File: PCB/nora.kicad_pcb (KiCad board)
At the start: 2 copper layers, 285 x 95.1 mm, 232 parts, among them J1 USB_C_Receptacle_USB2.0, J2 Conn_01x04, J3 Conn_01x02, J5 Conn_02x03_Odd_Even, U1 ATmega32U4-MU, U2 24LC64, U4 Pico, Y1 16MHz

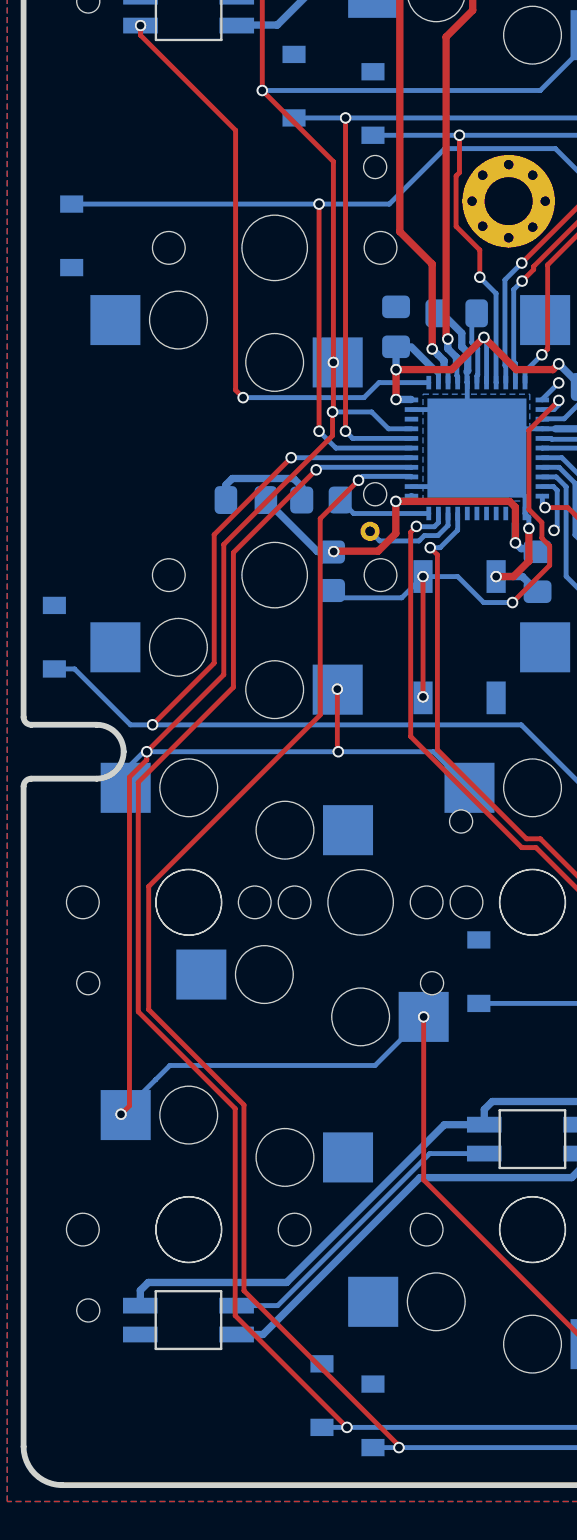
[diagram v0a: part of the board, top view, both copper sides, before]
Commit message: パスコンとRを入れ替えて、パスコンをMCUに近づけた#25
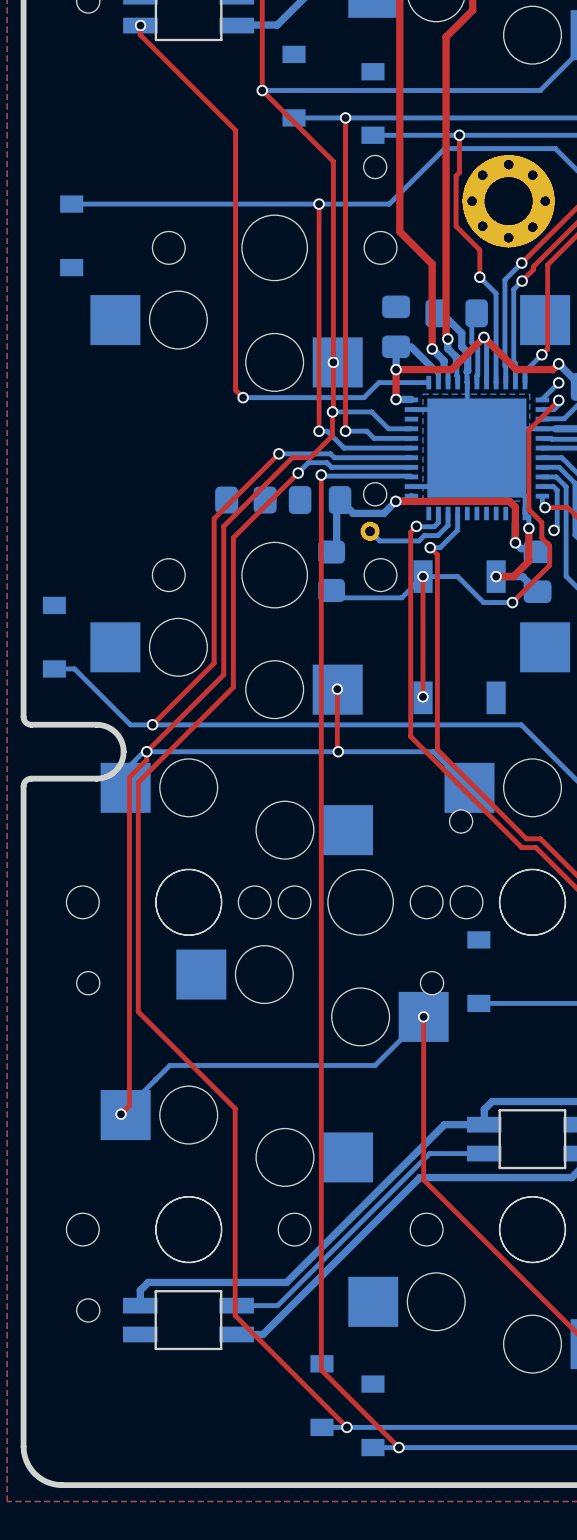
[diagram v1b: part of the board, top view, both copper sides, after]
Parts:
- moved R6 3.90 mm to (34.1, 66.0)
- moved C5 3.85 mm to (38.0, 66.0)
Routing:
- net row9: track 330.3 -> 324.2 mm
- net GND: track 612.4 -> 606.7 mm
- net Net-(R6-Pad2): track 4.89 -> 0.00 mm
- net +5V: track 88.9 -> 85.3 mm, vias 9 -> 8
- net row7: track 310.8 -> 311.4 mm
- net row4: track 338.1 -> 338.7 mm
- net col0: track 166.4 -> 166.9 mm

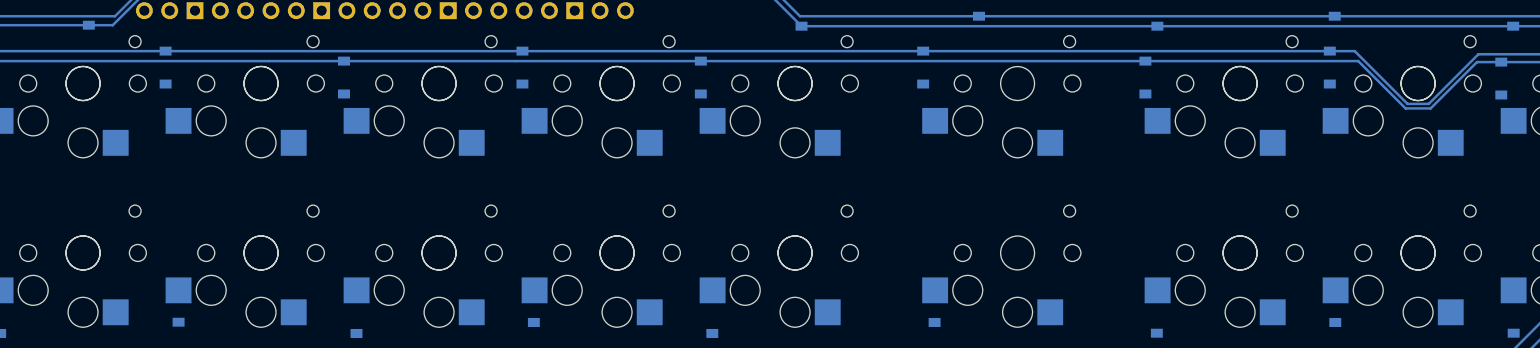
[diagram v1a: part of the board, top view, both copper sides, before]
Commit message: 中央、右上のネジ穴にかぶるスイッチにシルクを追加#14
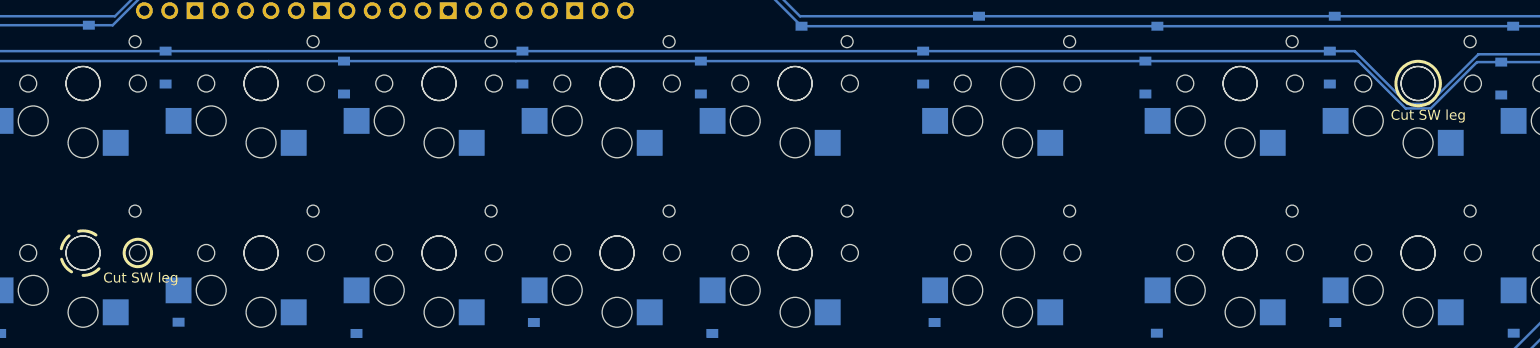
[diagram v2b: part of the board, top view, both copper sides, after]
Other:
- board text added: "Cut SW leg"

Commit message: URL added.#20
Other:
- board text added: "#Nora_kbd v.0.1 by @jpskenn, https://git.io/nora_kbd"
- board text removed: "#Nora_kbd v.0.1, by @jpskenn"

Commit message: Update and Change version information.#18#21
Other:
- board text added: "#Nora_kbd DN0020 by @jpskenn, https://git.io/nora_kbd"
- board text removed: "#Nora_kbd v.0.1 by @jpskenn, https://git.io/nora_kbd"

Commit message: WIP 配線
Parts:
- moved F1 0.77 mm to (50.9, 27.2)
- moved R1 0.77 mm to (50.2, 24.8)
- moved D10 0.57 mm to (31.4, 25.7)
- moved R3 0.50 mm to (43.1, 31.0)
- moved R2 0.40 mm to (27.2, 25.5)
- moved R4 0.39 mm to (43.1, 33.6)
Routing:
- net col7: track 0.00 -> 294.5 mm, vias 0 -> 10
- net col6: track 0.00 -> 245.2 mm, vias 0 -> 5
- net col5: track 0.00 -> 208.5 mm, vias 0 -> 5
- net col1: track 19.0 -> 207.9 mm, vias 0 -> 7
- net col3: track 0.00 -> 182.8 mm, vias 0 -> 5
- net col4: track 0.00 -> 176.1 mm, vias 0 -> 4
- net col2: track 3.00 -> 162.6 mm, vias 1 -> 6
- net RESET: track 30.4 -> 83.3 mm, vias 4 -> 6
- net Net-(J1-PadA5): track 0.00 -> 15.1 mm
- net row1: track 256.7 -> 270.4 mm, vias 1 -> 2
- net Net-(J1-PadB5): track 0.00 -> 10.9 mm
- net Net-(D10-Pad2): track 4.73 -> 15.5 mm
- net Net-(D10-Pad3): track 8.38 -> 17.2 mm
- net row4: track 338.7 -> 342.1 mm
- net +5V: track 85.3 -> 84.0 mm
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
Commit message: WIP 配線
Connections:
- U1 pad 21: col2 -> col3
- U1 pad 25: col3 -> col2
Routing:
- net col7: track 294.5 -> 530.2 mm
- net col6: track 245.2 -> 454.6 mm, vias 5 -> 8
- net col5: track 208.5 -> 376.6 mm, vias 5 -> 7
- net col4: track 176.1 -> 307.1 mm, vias 4 -> 6
- net col0: track 166.9 -> 284.3 mm, vias 10 -> 11
- net col2: track 162.6 -> 272.9 mm, vias 6 -> 8
- net col3: track 182.8 -> 274.8 mm, vias 5 -> 7
- net col1: track 207.9 -> 296.8 mm, vias 7 -> 8
- net row9: track 324.2 -> 397.0 mm, vias 2 -> 3
- net row4: track 342.1 -> 408.7 mm, vias 2 -> 3
- net row8: track 286.8 -> 330.8 mm, vias 2 -> 3
- net row3: track 293.8 -> 335.0 mm, vias 2 -> 3
- net +5V: track 84.0 -> 124.3 mm, vias 8 -> 11
- net row7: track 311.4 -> 351.3 mm, vias 2 -> 3
- net row2: track 267.2 -> 305.1 mm, vias 2 -> 3
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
